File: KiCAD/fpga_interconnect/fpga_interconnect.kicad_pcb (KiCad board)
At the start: 2 copper layers, 46.5 x 42.5 mm, 3 parts, among them J1 VGA, J2 Pmod 1, J3 Pmod 2

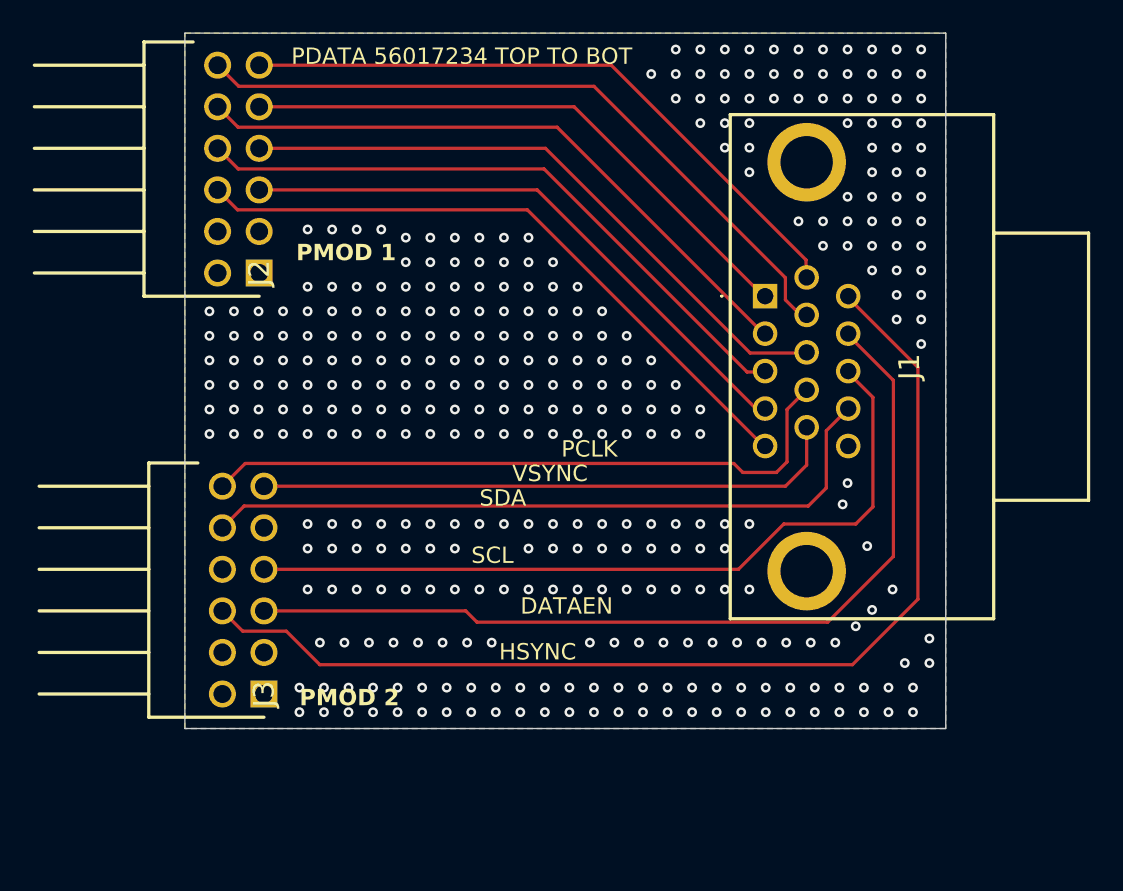
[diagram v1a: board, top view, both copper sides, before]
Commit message: Complete FPGA interconnect
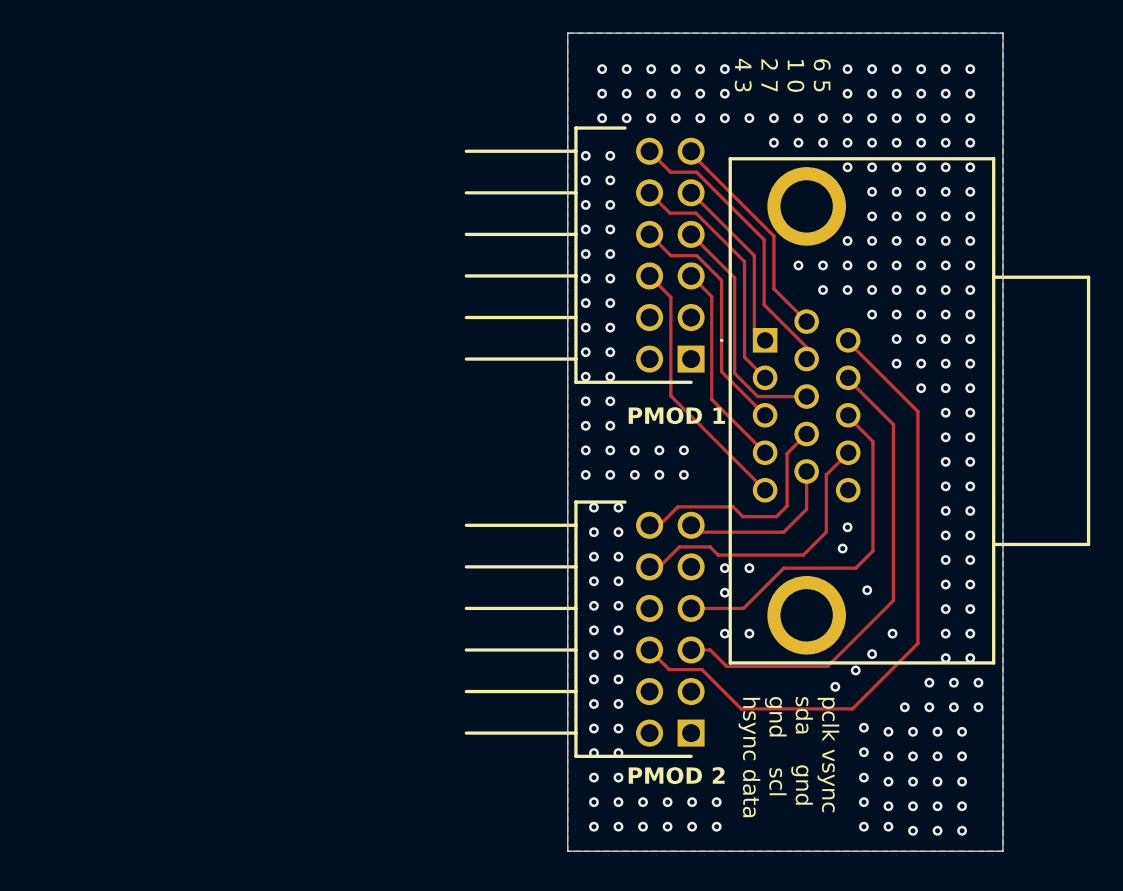
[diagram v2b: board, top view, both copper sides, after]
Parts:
- moved J2 26.9 mm to (171.9, 93.9)
- moved J3 26.2 mm to (171.9, 116.8)
- moved J1 2.70 mm to (176.5, 92.8)
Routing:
- net /PDATA5: track 39.8 -> 13.5 mm
- net /PCLK: track 40.5 -> 14.1 mm
- net /IIC1_SCL: track 47.7 -> 21.4 mm
- net /IIC1_SDA: track 43.3 -> 17.3 mm
- net /HSYNC: track 65.8 -> 39.8 mm
- net /DATAEN_CMD: track 55.1 -> 29.2 mm
- net /VSYNC: track 36.0 -> 10.1 mm
- net /PDATA6: track 43.0 -> 17.6 mm
- net /PDATA0: track 35.7 -> 10.9 mm
- net /PDATA4: track 39.9 -> 16.0 mm
- net /PDATA1: track 39.2 -> 15.3 mm
- net /PDATA2: track 39.1 -> 15.5 mm
- net /PDATA3: track 36.4 -> 13.3 mm
- net /PDATA7: track 38.0 -> 15.0 mm
- net GND: vias 352 -> 238
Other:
- board size 46.5 x 42.5 mm -> 26.6 x 50 mm
- board text added: "${REFERENCE}"
- board text added: "6 5 1 0 2 7 4 3"
- board text added: "pclk vsync sda gnd gnd scl hsync data"
- board text removed: "DATAEN"
- board text removed: "HSYNC"
- board text removed: "PCLK"
- board text removed: "PDATA 56017234 TOP TO BOT"
- board text removed: "SCL"
- board text removed: "SDA"
- board text removed: "VSYNC"

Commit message: productino files
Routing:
- net /PDATA3: track 13.3 -> 12.7 mm
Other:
- board text removed: "${REFERENCE}"

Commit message: production file updates
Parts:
- added G***: LOGO, LOGO, B.Cu at (181.7, 117.9)
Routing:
- net GND: vias 238 -> 175
